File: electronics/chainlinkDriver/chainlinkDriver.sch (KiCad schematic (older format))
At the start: 66 parts, among them J10 Sensor, J11 Sensor, J12 Motor, J13 Motor, J14 Sensor, J15 Sensor, J16 Power, J17 Power, J18 Power, J19 IDC, J20 IDC, J3 Motor, J5 Motor, J6 Motor, J7 Motor, J8 Sensor, J9 Sensor, U1 74HC595, U10 TPL7407L, U2 TPL7407L, U3 74HC125, U4 74HC165, U5 74HC595, U6 TPL7407L, U7 74HC595, U8 TPL7407L, U9 74HC595

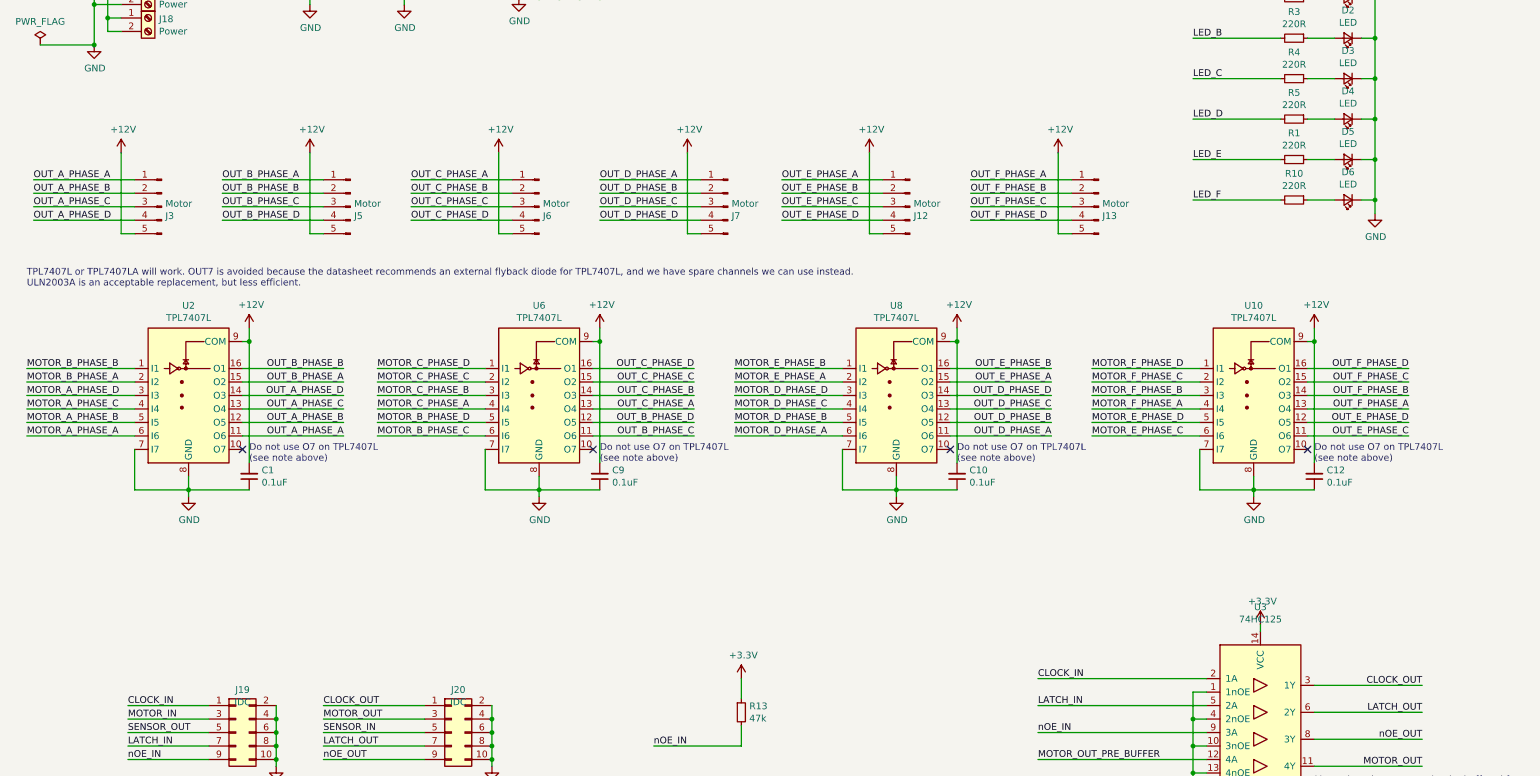
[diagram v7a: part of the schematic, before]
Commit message: More tweaks to Chainlink Driver, update Chainlink Buddy
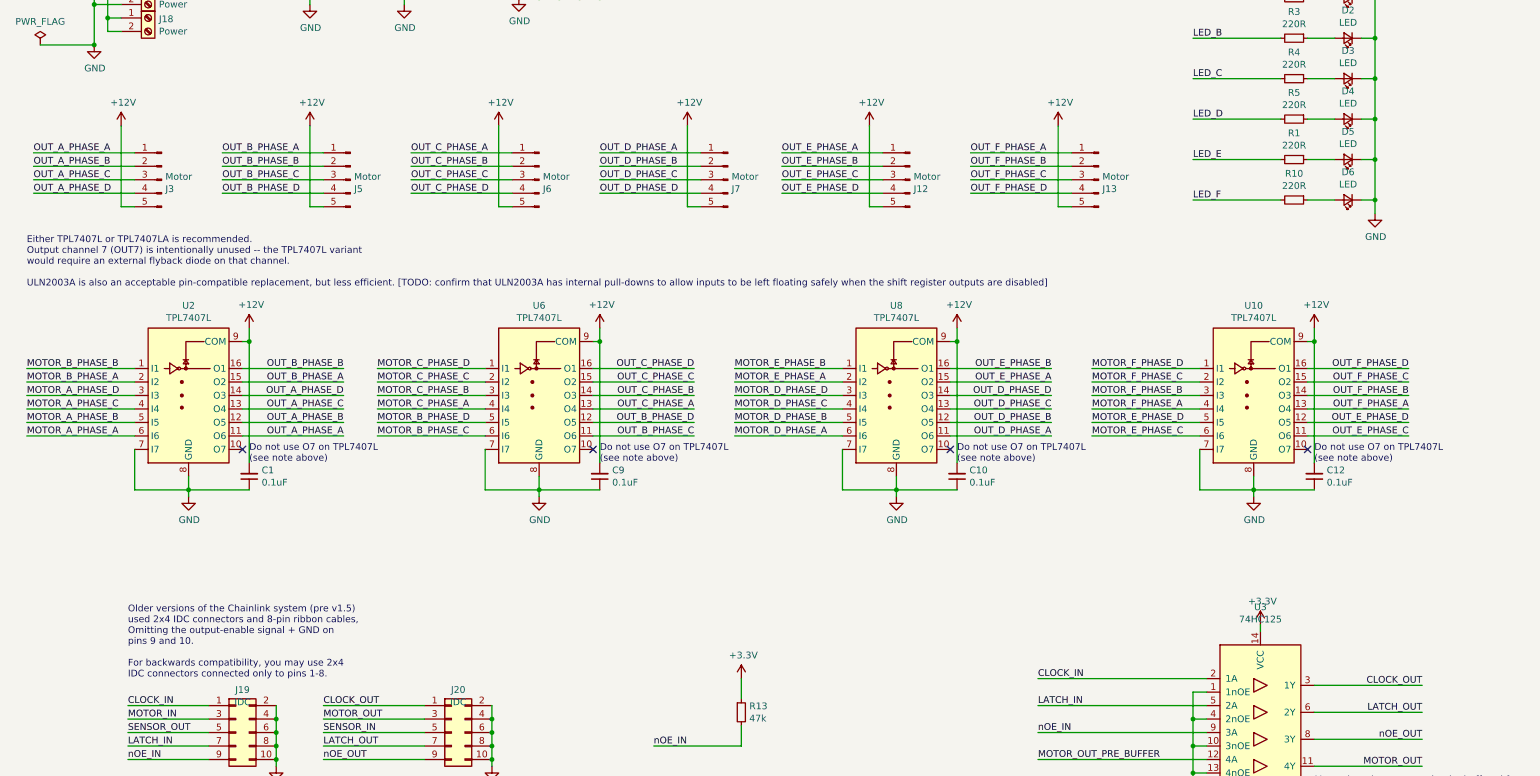
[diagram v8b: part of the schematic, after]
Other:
- note added: "Either TPL7407L or TPL7407LA is recommended.\nOutput channel 7 (OUT7) is intentionally unused -- the TPL7407L variant\nwould require an external flyback diode on that channel.\n\nULN2003A is also an acceptable pin-compatible replacement, but less efficient. [TODO: confirm that ULN2003A has internal pull-downs to allow inputs to be left floating safely when the shift register outputs are disabled]"
- note added: "Older versions of the Chainlink system (pre v1.5)\nused 2x4 IDC connectors and 8-pin ribbon cables,\nOmitting the output-enable signal + GND on \npins 9 and 10.\n\nFor backwards compatibility, you may use 2x4 \nIDC connectors connected only to pins 1-8."
- note removed: "TPL7407L or TPL7407LA will work. OUT7 is avoided because the datasheet recommends an external flyback diode for TPL7407L, and we have spare channels we can use instead.\nULN2003A is an acceptable replacement, but less efficient."
- moved on the sheet: J12, J13, J3, J5, J6, J7
